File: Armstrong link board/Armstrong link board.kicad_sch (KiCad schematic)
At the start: 8 parts, among them J1 Camera, J2 Wheelson, J3 Armstrong, J4 Conn_01x03_Pin, J5 JST 2.0, J6 USB_C_Receptacle_USB2.0_16P

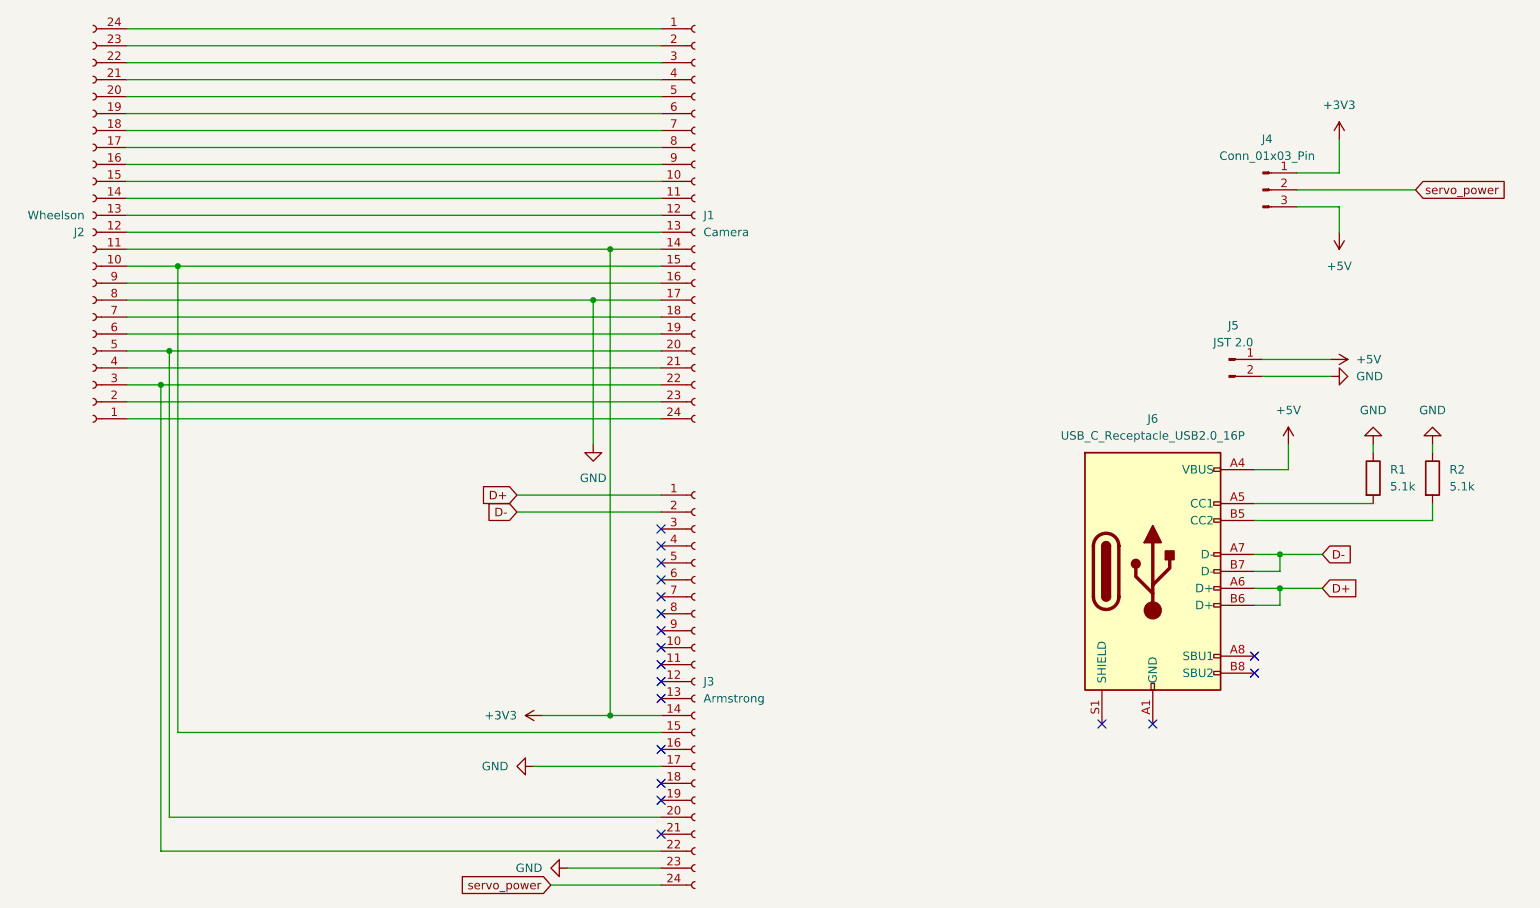
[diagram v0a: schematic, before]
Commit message: connect ground and shield from usb
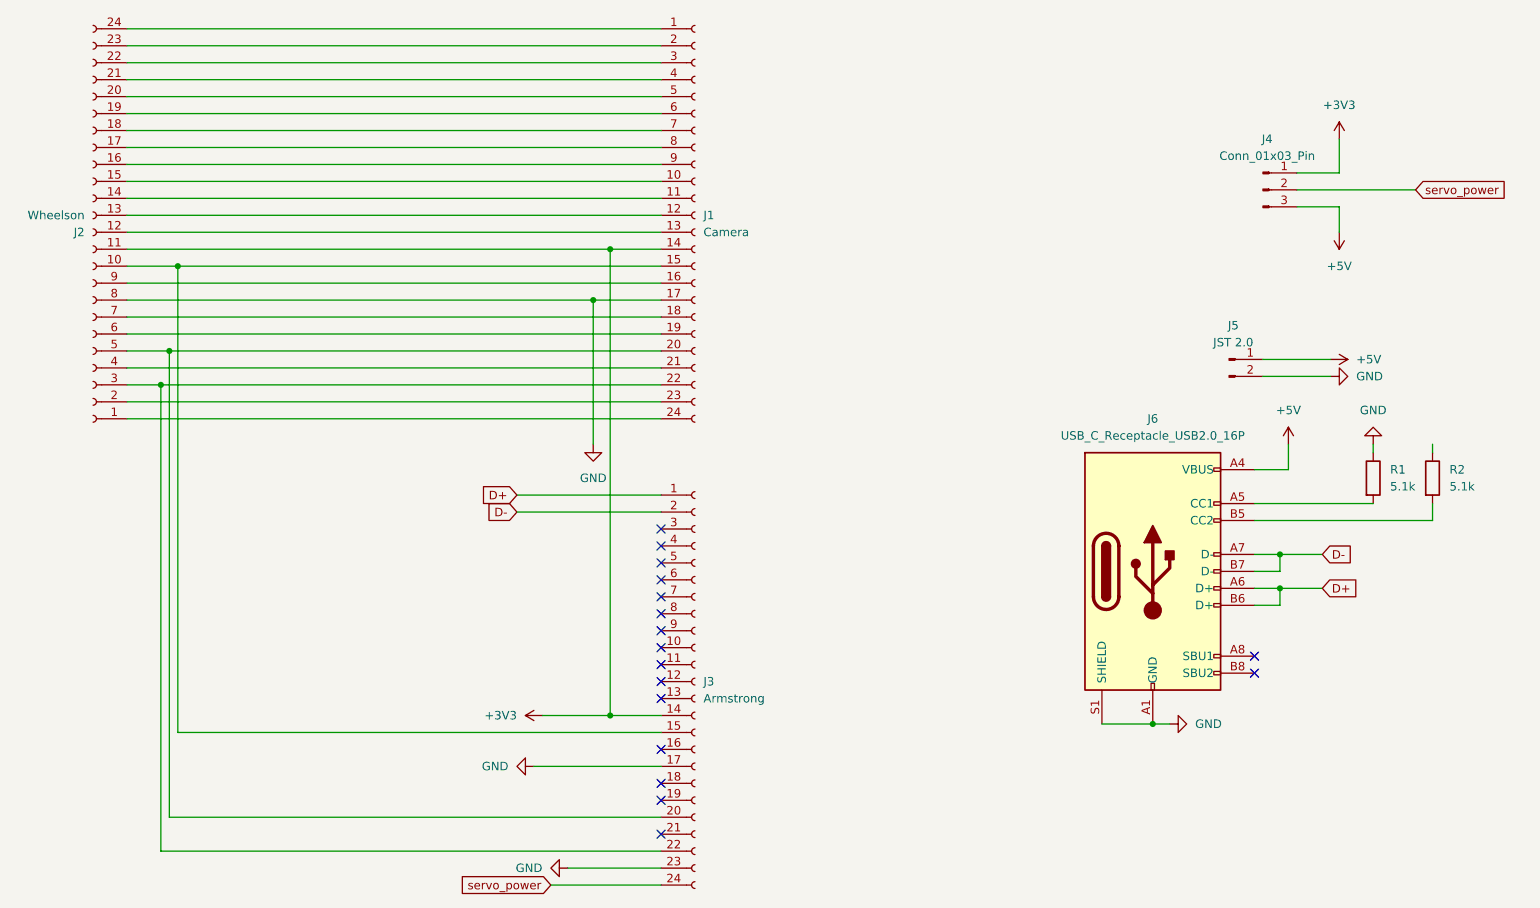
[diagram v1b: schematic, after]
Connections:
- net GND: now also J6.A1 (GND), J6.A12 (GND), J6.B1 (GND), J6.B12 (GND), J6.S1 (SHIELD); no longer R2.1
- no-connect marks 19 -> 17
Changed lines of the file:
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@@
 (kicad_sch
-	(version 20231120)
+	(version 20250114)
 	(generator "eeschema")
-	(generator_version "8.0")
+	(generator_version "9.0")
 	(paper "A4")
 	(junction
@@
 		(color 0 0 0 0)
 	)
+	(junction
+		(at 205.74 163.83)
+		(diameter 0)
+		(color 0 0 0 0)
+	)
 	(no_connect
 		(at 132.08 152.4)
@@
 	)
 	(no_connect
-		(at 205.74 163.83)
-	)
-	(no_connect
 		(at 220.98 156.21)
 	)
@@
 		(at 132.08 160.02)
 	)
-	(no_connect
-		(at 198.12 163.83)
-	)
 	(wire
 		(pts
@@
 	(wire
 		(pts
+			(xy 198.12 163.83) (xy 205.74 163.83)
+		)
+		(stroke
+			(width 0)
+			(type default)
+		)
+	)
+	(wire
+		(pts
 			(xy 220.98 146.05) (xy 224.79 146.05)
 		)
@@
 		(pts
 			(xy 124.46 162.56) (xy 132.08 162.56)
+		)
+		(stroke
+			(width 0)
+			(type default)
+		)
+	)
+	(wire
+		(pts
+			(xy 208.28 163.83) (xy 205.74 163.83)
 		)
 		(stroke
@@
 	(symbol
 		(lib_id "power:GND")
-		(at 247.65 121.92 180)
+		(at 208.28 163.83 90)
 		(unit 1)
 		(exclude_from_sim no)
@@
 		(fields_autoplaced yes)
 		(property "Reference" "#PWR03"
-			(at 247.65 115.57 0)
+			(at 214.63 163.83 0)
 			(effects
 				(font
@@
 		)
 		(property "Value" "GND"
-			(at 247.65 116.84 0)
-			(effects
-				(font
-					(size 1.27 1.27)
-				)
+			(at 212.09 163.8299 90)
+			(effects
+				(font
+					(size 1.27 1.27)
+				)
+				(justify right)
 			)
 		)
 		(property "Footprint" ""
-			(at 247.65 121.92 0)
+			(at 208.28 163.83 0)
 			(effects
 				(font
@@
 		)
 		(property "Datasheet" ""
-			(at 247.65 121.92 0)
+			(at 208.28 163.83 0)
 			(effects
 				(font
@@
 		)
 		(property "Description" "Power symbol creates a global label with name \"GND\" , ground"
-			(at 247.65 121.92 0)
+			(at 208.28 163.83 0)
 			(effects
 				(font
@@
 		)
 	)
+	(embedded_fonts no)
 )
